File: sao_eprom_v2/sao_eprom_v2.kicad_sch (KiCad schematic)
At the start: 36 parts, among them J1 Conn_01x03, J2 USB_C_Receptacle_USB2.0, J3 sao_v2_addon_tht, J4 Conn_01x02, U1 W25Q128JVS, U2 RP2040, U3 24LC00, X1 SX3M12.000M20F30TNN

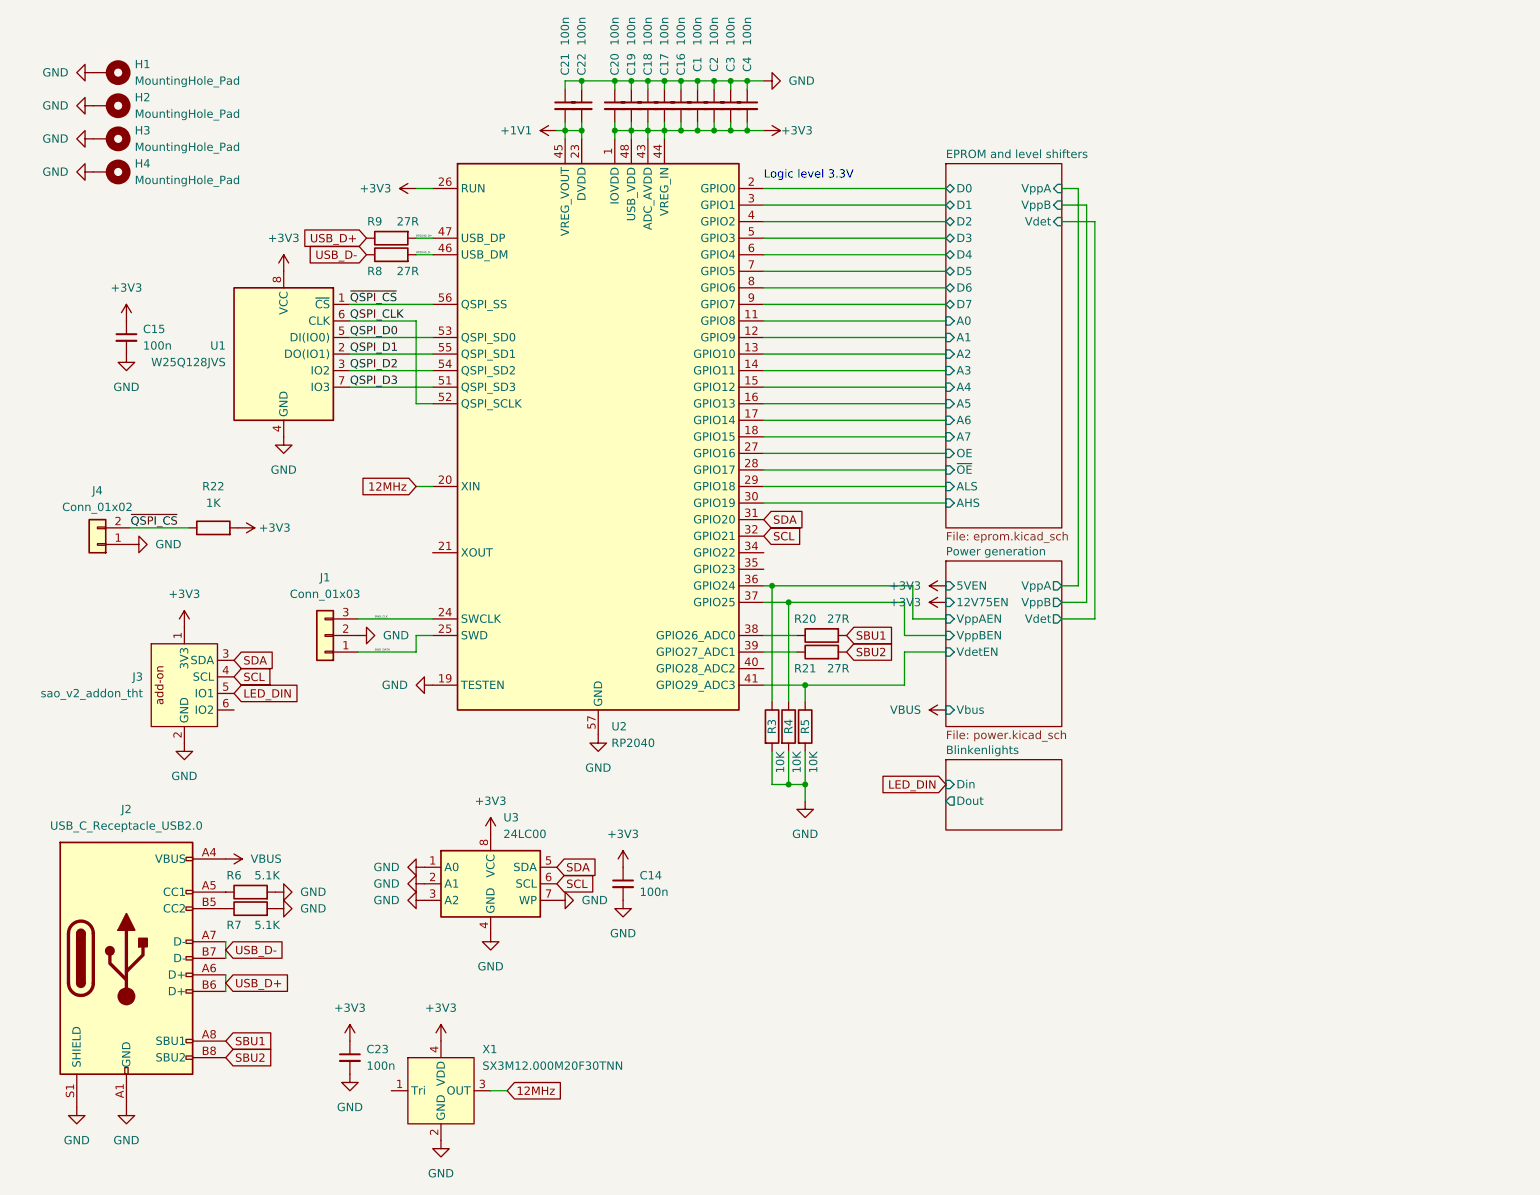
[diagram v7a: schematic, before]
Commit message: Now with QWIIC and TestPads!
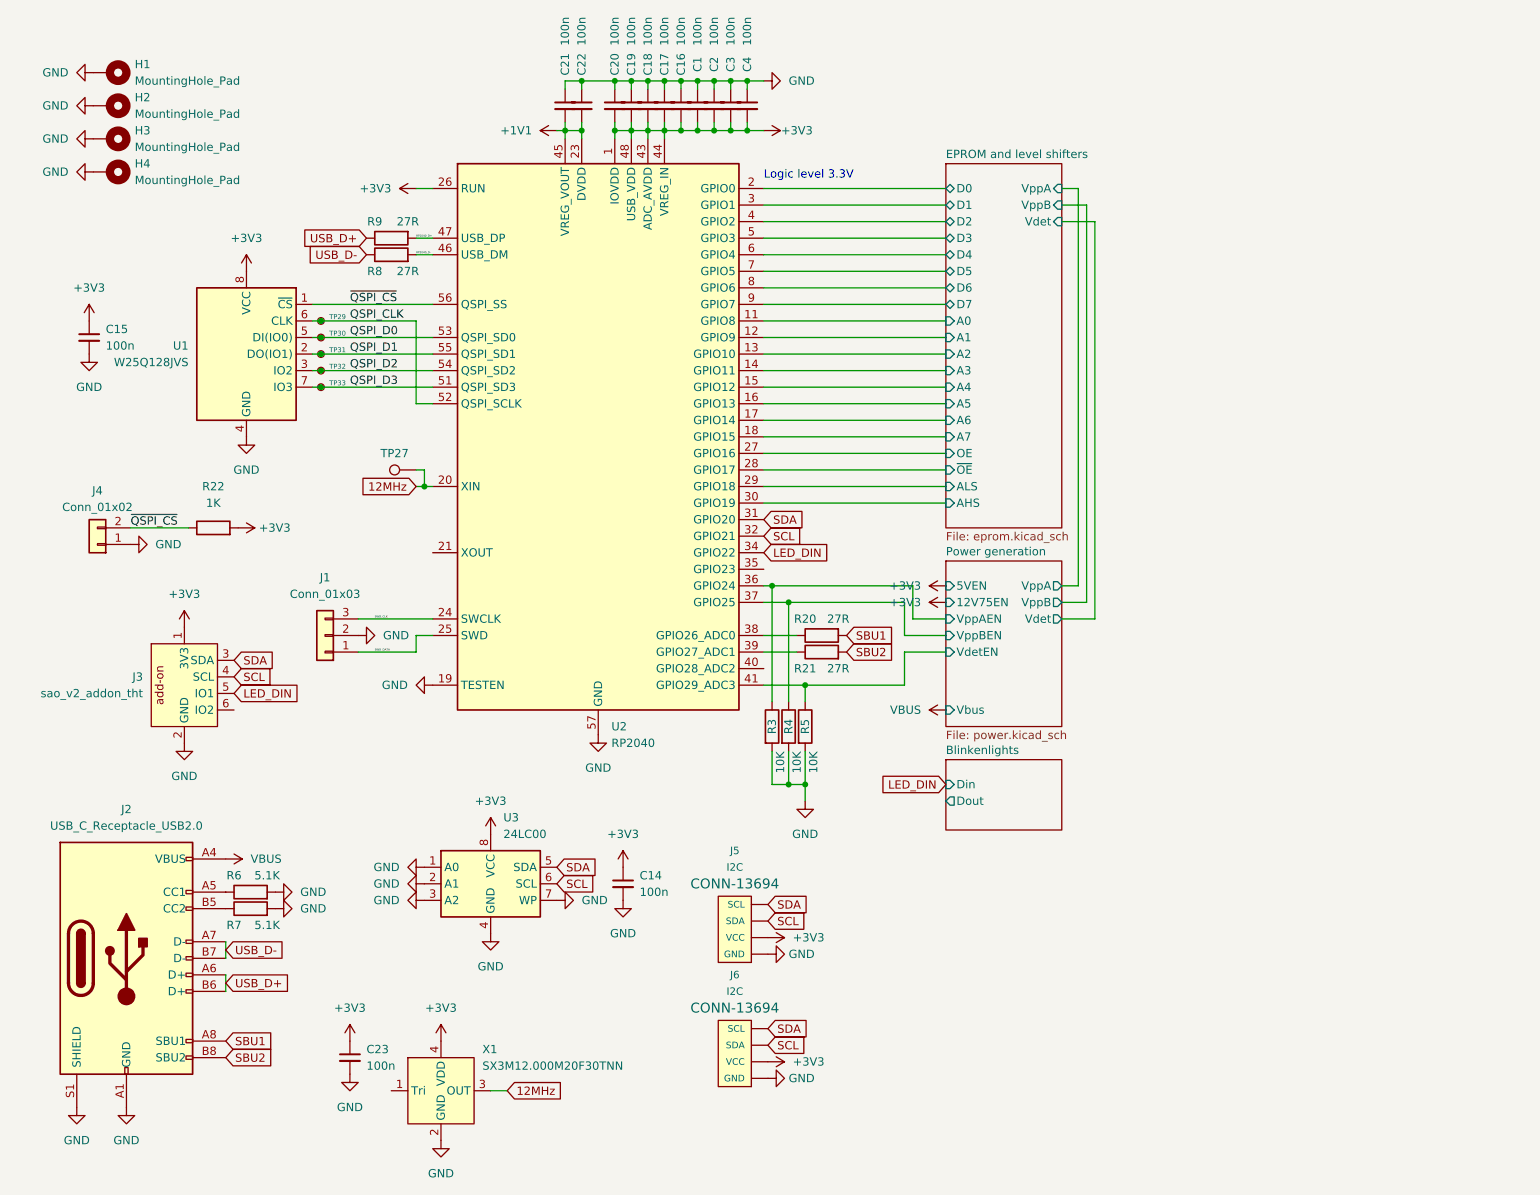
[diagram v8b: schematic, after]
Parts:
- added J5, J6: I2C, qwiic:1X04_1MM_RA_GND, symbol qwiic:qwiic
- added TP27: TestPoint, TestPoint:TestPoint_Pad_D1.0mm, symbol Connector:TestPoint
- added TP29, TP30, TP31, TP32, TP33: TestPoint_Small, TestPoint:TestPoint_Pad_D1.0mm, symbol Connector:TestPoint_Small
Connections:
- net +3V3: now also J5.2 (VCC), J6.2 (VCC)
- net 12MHz: now also TP27.1
- net GND: now also J5.1 (GND), J5.5, J5.6, J6.1 (GND), J6.5, J6.6
- net LED_DIN: now also U2.34 (GPIO22)
- net QSPI_CLK: now also TP29.1
- net QSPI_D0: now also TP30.1
- net QSPI_D1: now also TP31.1
- net QSPI_D2: now also TP32.1
- net QSPI_D3: now also TP33.1
- net SCL: now also J5.3 (SDA), J6.3 (SDA)
- net SDA: now also J5.4 (SCL), J6.4 (SCL)
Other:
- moved on the sheet: C15, U1
